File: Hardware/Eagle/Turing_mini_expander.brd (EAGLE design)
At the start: 106 x 19.5 mm, 20 parts, among them U1 TL072_

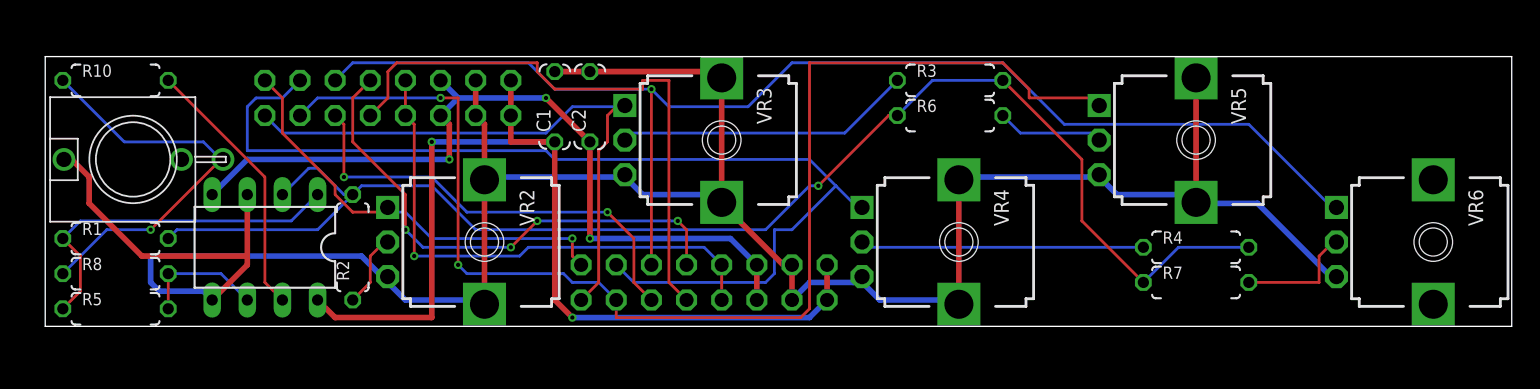
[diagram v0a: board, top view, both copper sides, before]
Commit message: Thonkiconn error corrected and re-routed
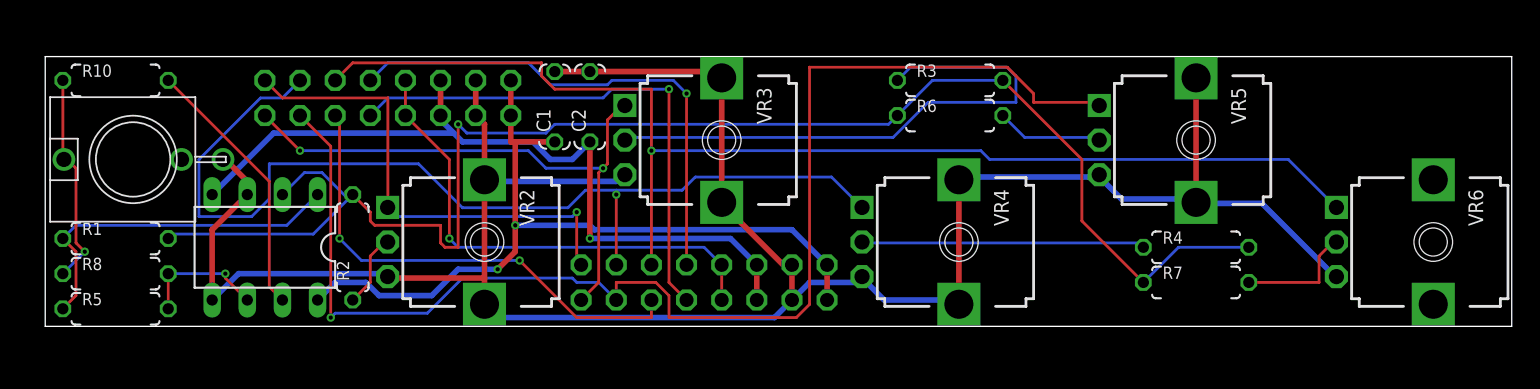
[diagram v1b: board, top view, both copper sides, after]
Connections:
- net GND: now also MAIN_OUT.P$3_SLEEVE; no longer MAIN_OUT.P$1
- net N$5: now also MAIN_OUT.P$1_TIP; no longer MAIN_OUT.P$3
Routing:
- net N$16: track 21.8 -> 40.6 mm
- net +12V: track 72.7 -> 58.3 mm
- net N$5: track 28.9 -> 15.5 mm
- net GND: track 188.0 -> 177.4 mm
- net SUM: track 101.8 -> 108.8 mm
- net GATE8: track 42.5 -> 38.1 mm, vias 0 -> 1
- net GATE1: track 31.4 -> 35.3 mm
- net GATE5: track 92.5 -> 88.6 mm
- net GATE4: track 92.4 -> 95.2 mm, vias 2 -> 1
- net CLOCK: track 38.5 -> 35.8 mm
- net GATE6: track 32.5 -> 35.2 mm
- net GATE3: track 75.0 -> 73.3 mm, vias 0 -> 1
- net GATE2: track 43.0 -> 41.5 mm, vias 0 -> 2
- net -12V: track 58.4 -> 57.0 mm, vias 3 -> 1
- net GATE7: track 37.3 -> 37.0 mm, vias 4 -> 1
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
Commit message: Fixes after first photo
Fixes #2, fixes #3, fixes #4
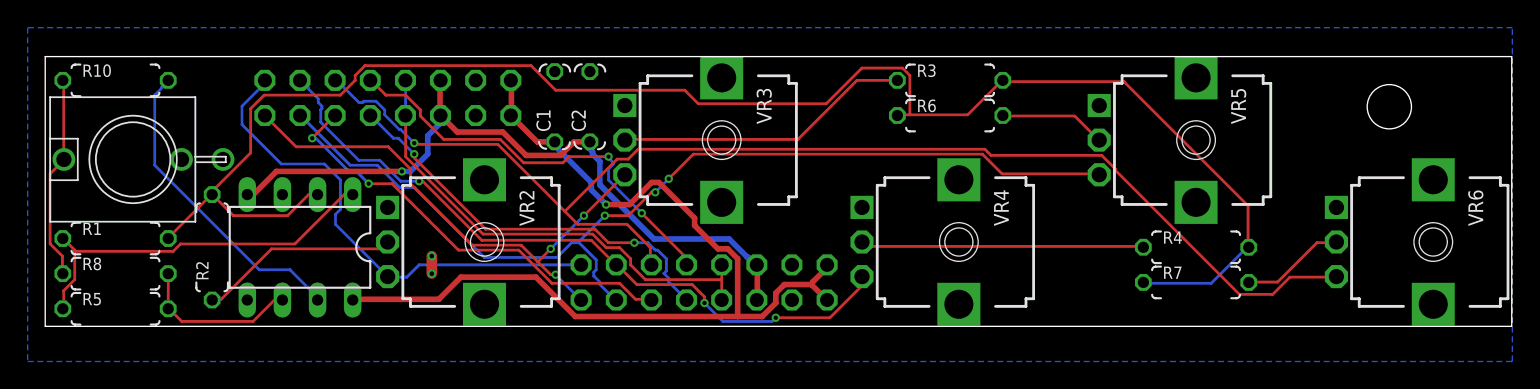
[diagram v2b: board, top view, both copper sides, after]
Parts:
- added U$1: (no value), MusicThingModular:MOUNTING_HOLE
- moved R2 10.2 mm to (12.1, 5.71)
- moved U1 2.54 mm to (18.4, 5.71)
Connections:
- net GATE1: now also VR2.3; no longer VR2.1
- net GATE2: now also VR3.3; no longer VR3.1
- net GATE3: now also VR4.3; no longer VR4.1
- net GATE4: now also VR5.3; no longer VR5.1
- net GATE5: now also VR6.3; no longer VR6.1
- net GND: now also VR2.1, VR2.CHASSIS2, VR3.1, VR3.CHASSIS2, VR4.1, VR4.CHASSIS2, VR5.1, VR5.CHASSIS2, VR6.1, VR6.CHASSIS2; no longer VR2.3, VR2.M1, VR2.M2, VR3.3, VR3.M1, VR3.M2, VR4.3, VR4.M1, VR4.M2, VR5.3, VR5.M1, VR5.M2, VR6.3
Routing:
- net GND: track 177.4 -> 1.27 mm, vias 0 -> 2
- net GATE4: track 95.2 -> 71.2 mm, vias 1 -> 3
- net GATE3: track 73.3 -> 50.8 mm, vias 1 -> 3
- net N$16: track 40.6 -> 21.5 mm
- net +12V: track 58.3 -> 69.5 mm, vias 2 -> 1
- net N$2: track 5.36 -> 14.4 mm
- net GATE8: track 38.1 -> 29.6 mm, vias 1 -> 2
- net SUM: track 108.8 -> 117.2 mm, vias 1 -> 0
- net GATE7: track 37.0 -> 30.6 mm, vias 1 -> 2
- net -12V: track 57.0 -> 52.3 mm
- net GATE2: track 41.5 -> 37.9 mm, vias 2 -> 3
- net GATE6: track 35.2 -> 31.7 mm
- net GATE5: track 88.6 -> 91.9 mm
- net N$6: track 19.3 -> 22.5 mm
- net N$4: track 9.23 -> 11.8 mm, vias 1 -> 0
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- added copper zone on layer 16, net GND
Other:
- board text added: "Turing Machine Mini Voltage Expander Designed in Portscatho Cornwall by Tom Whitwell PCB rev 2 September 2015 musicthing.co.uk"
- board text removed: "Turing Machine Mini Voltage Expander Designed in Portscatho Cornwall by Tom Whitwell PCB rev 1 August 2015 musicthing.co.uk"

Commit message: Add vector logo to back of board
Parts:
- added U$2: (no value), MusicThingModular:MTM_1CM_LOGO_WHITE
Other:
- board text removed: "MUSIC THING MODULAR"

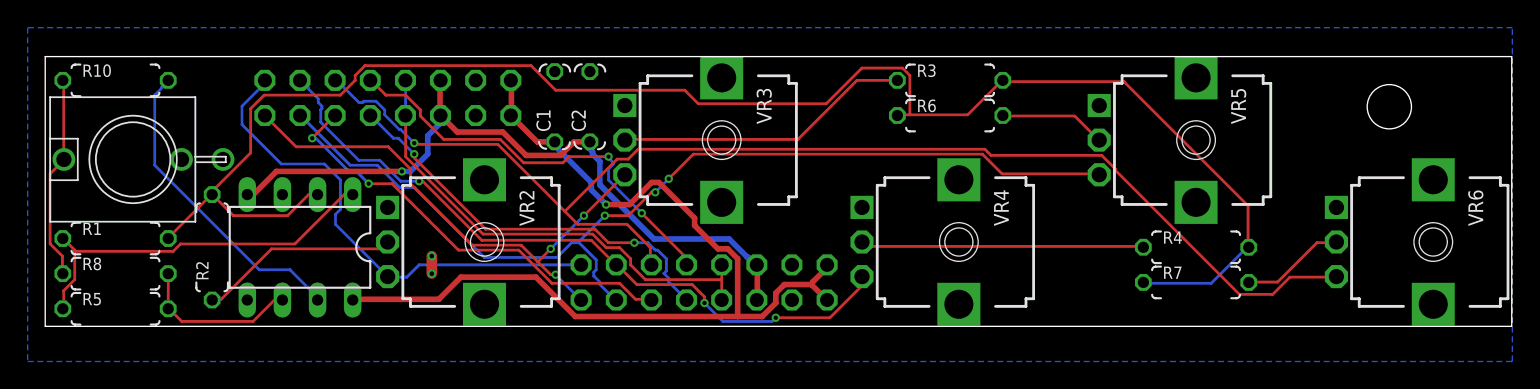
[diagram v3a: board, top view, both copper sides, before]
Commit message: reroute fatter traces
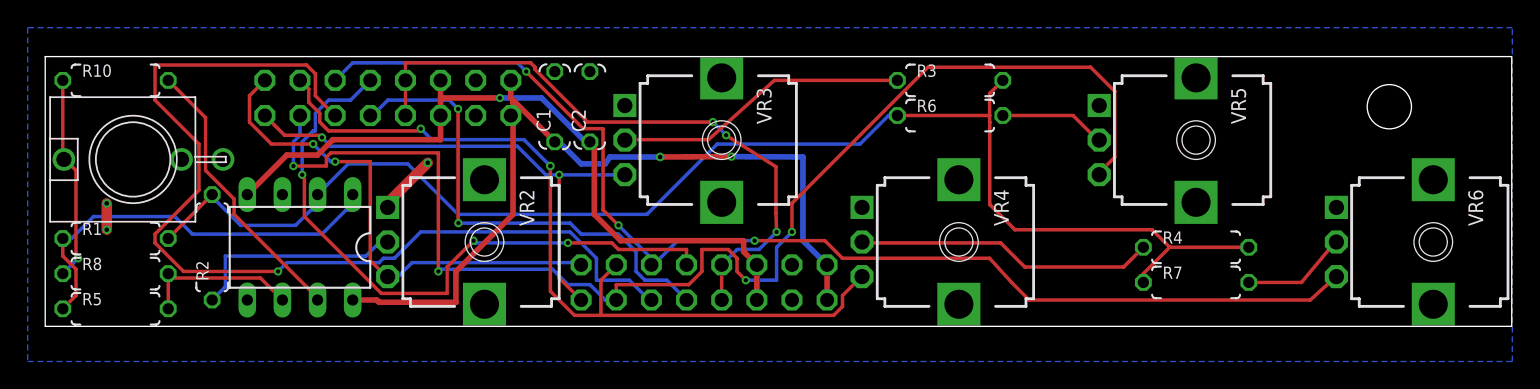
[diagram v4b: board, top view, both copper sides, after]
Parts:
- removed U$2: (no value), MusicThingModular:MTM_1CM_LOGO_WHITE
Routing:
- net GATE6: track 31.7 -> 71.8 mm, vias 2 -> 1
- net GATE4: track 71.2 -> 94.3 mm, vias 3 -> 4
- net GATE7: track 30.6 -> 47.0 mm, vias 2 -> 3
- net SUM: track 117.2 -> 101.4 mm
- net CLOCK: track 34.9 -> 45.8 mm, vias 0 -> 3
- net +12V: track 69.5 -> 59.6 mm, vias 1 -> 2
- net GATE3: track 50.8 -> 59.8 mm, vias 3 -> 2
- net GATE5: track 91.9 -> 85.7 mm, vias 1 -> 3
- net GATE8: track 29.6 -> 35.0 mm
- net GND: track 1.27 -> 6.33 mm, vias 2 -> 3
- net N$15: track 27.6 -> 29.8 mm
- net N$6: track 22.5 -> 20.3 mm
- net -12V: track 52.3 -> 53.6 mm
- net N$2: track 14.4 -> 15.7 mm
- net N$19: track 20.5 -> 21.7 mm
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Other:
- board text added: "RED>> RED>>"
- board text removed: "RED>>RED>>"

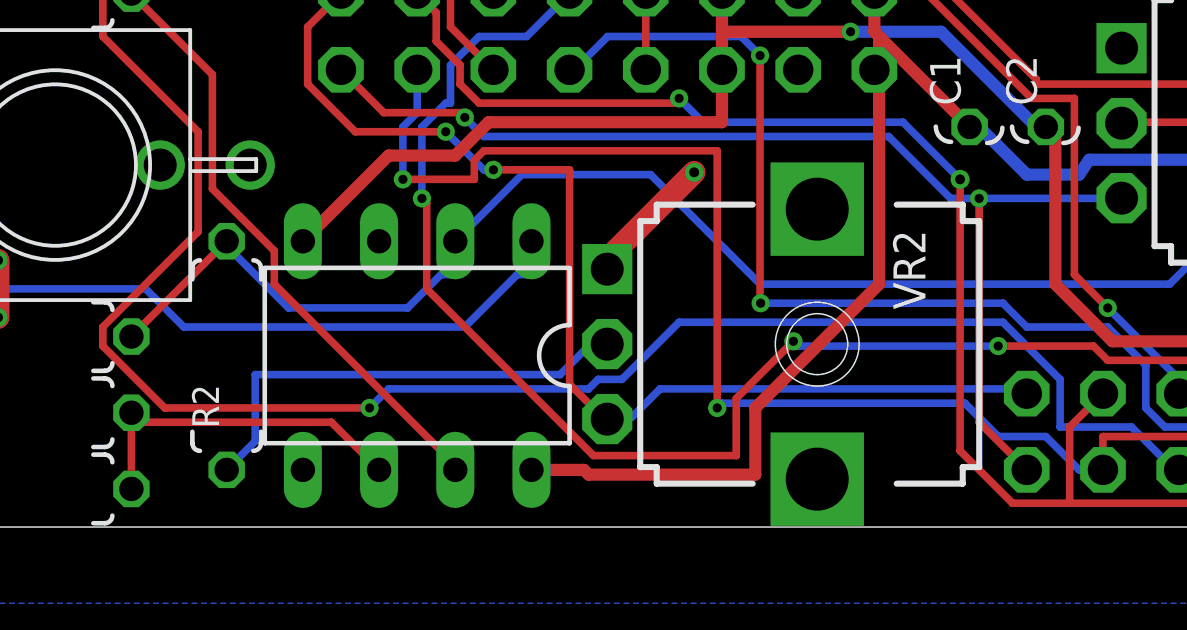
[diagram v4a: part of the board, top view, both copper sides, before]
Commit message: Rev 2 Board and Panel complete and prototypes ordered
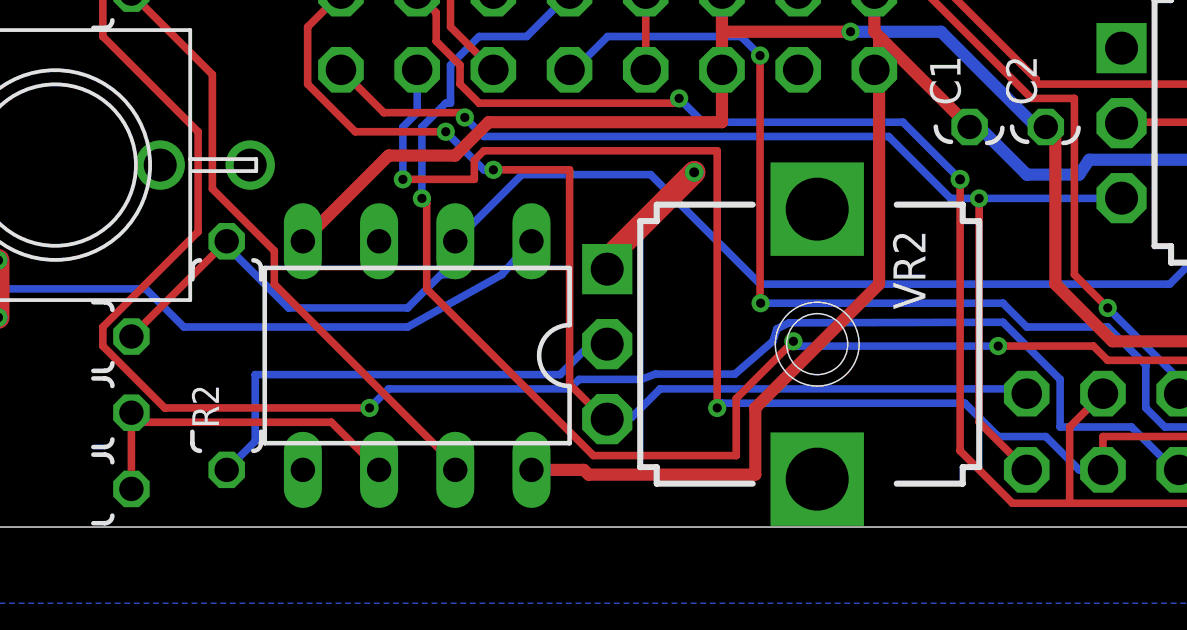
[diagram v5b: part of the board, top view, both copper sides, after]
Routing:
- net N$15: track 29.8 -> 29.0 mm
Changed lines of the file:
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@@
 <setting verticaltext="up"/>
 </settings>
-<grid distance="25" unitdist="mil" unit="mil" style="lines" multiple="1" display="no" altdistance="3.5" altunitdist="mil" altunit="mil"/>
+<grid distance="25" unitdist="mil" unit="mil" style="lines" multiple="1" display="no" altdistance="4" altunitdist="mil" altunit="mil"/>
 <layers>
 <layer number="1" name="Top" color="4" fill="1" visible="yes" active="yes"/>
@@
 <layer number="42" name="bRestrict" color="1" fill="10" visible="yes" active="yes"/>
 <layer number="43" name="vRestrict" color="2" fill="10" visible="yes" active="yes"/>
-<layer number="44" name="Drills" color="7" fill="1" visible="no" active="yes"/>
-<layer number="45" name="Holes" color="7" fill="1" visible="no" active="yes"/>
+<layer number="44" name="Drills" color="7" fill="1" visible="yes" active="yes"/>
+<layer number="45" name="Holes" color="7" fill="1" visible="yes" active="yes"/>
 <layer number="46" name="Milling" color="3" fill="1" visible="yes" active="yes"/>
 <layer number="47" name="Measures" color="7" fill="1" visible="yes" active="yes"/>
@@
 <wire x1="106" y1="19.5" x2="0" y2="19.5" width="0" layer="20"/>
 <wire x1="0" y1="19.5" x2="0" y2="0" width="0" layer="20"/>
-<text x="11.267440625" y="18.93061875" size="1.27" layer="22" font="vector" ratio="15" rot="SMR270" align="top-left">RED&gt;&gt;
+<text x="13.807440625" y="13.85061875" size="1.27" layer="22" font="vector" ratio="15" rot="SMR90" align="top-left">RED&gt;&gt;
 RED&gt;&gt;</text>
 <text x="92.32265" y="0.27305" size="1.016" layer="22" font="vector" rot="SMR90" align="top-left">Turing Machine
@@
 DO NOT CONNECT
 TO CASE POWER</text>
-<text x="34.127440625" y="5.59561875" size="1.27" layer="22" font="vector" ratio="15" rot="SMR270" align="top-left">RED&gt;&gt;
+<text x="36.667440625" y="0.51561875" size="1.27" layer="22" font="vector" ratio="15" rot="SMR90" align="top-left">RED&gt;&gt;
 RED&gt;&gt;</text>
 <text x="52.705" y="7.62" size="1.016" layer="22" rot="SMR90">Either header
 will work! </text>
-<polygon width="0" layer="22">
+<polygon width="0.0508" layer="22">
 <vertex x="71.42605625" y="18.5256625"/>
 <vertex x="70.942440625" y="18.5256625"/>
@@
 <vertex x="71.434690625" y="18.517028125"/>
 </polygon>
-<polygon width="0" layer="22">
+<polygon width="0.0508" layer="22">
 <vertex x="71.521053125" y="15.865775"/>
 <vertex x="71.50378125" y="15.632603125"/>
@@
 <vertex x="71.49514375" y="15.883046875"/>
 </polygon>
-<polygon width="0" layer="22">
+<polygon width="0.0508" layer="22">
 <vertex x="67.81620625" y="15.883046875"/>
 <vertex x="68.377546875" y="15.883046875"/>
@@
 <vertex x="67.81620625" y="15.891684375"/>
 </polygon>
-<polygon width="0" layer="22">
+<polygon width="0.0508" layer="22">
 <vertex x="72.617825" y="14.199028125"/>
 <vertex x="67.81620625" y="14.199028125"/>
@@
 <vertex x="72.617825" y="13.335428125"/>
 </polygon>
-<polygon width="0" layer="22">
+<polygon width="0.0508" layer="22">
 <vertex x="68.230734375" y="12.143659375"/>
 <vertex x="67.9975625" y="11.988209375"/>
@@
 <vertex x="68.2134625" y="12.135021875"/>
 </polygon>
-<polygon width="0" layer="22">
+<polygon width="0.0508" layer="22">
 <vertex x="72.617825" y="9.362865625"/>
 <vertex x="71.0978875" y="9.362865625"/>
@@
 <vertex x="72.6091875" y="9.371503125"/>
 </polygon>
-<polygon width="0" layer="22">
+<polygon width="0.0508" layer="22">
 <vertex x="67.764390625" y="8.87925"/>
 <vertex x="68.4293625" y="8.87925"/>
@@
 <vertex x="67.7816625" y="8.87925"/>
 </polygon>
-<polygon width="0" layer="22">
+<polygon width="0.0508" layer="22">
 <vertex x="71.512415625" y="6.04664375"/>
 <vertex x="70.873353125" y="6.04664375"/>
@@
 <vertex x="71.50378125" y="6.055278125"/>
 </polygon>
-<polygon width="0" layer="22">
+<polygon width="0.0508" layer="22">
 <vertex x="71.512415625" y="6.04664375"/>
 <vertex x="71.48650625" y="5.7875625"/>
@@
 <vertex x="70.85608125" y="6.04664375"/>
 </polygon>
-<polygon width="0" layer="22">
+<polygon width="0.0508" layer="22">
 <vertex x="72.617825" y="1.78909375"/>
 <vertex x="71.48650625" y="2.00499375"/>
@@
 <vertex x="72.617825" y="0.441878125"/>
 </polygon>
-<polygon width="0" layer="22">
+<polygon width="0.0508" layer="22">
 <vertex x="73.049625" y="11.815490625"/>
 <vertex x="73.749140625" y="11.815490625"/>
@@
 <vertex x="73.049625" y="11.8414"/>
 </polygon>
-<polygon width="0" layer="22">
+<polygon width="0.0508" layer="22">
 <vertex x="73.049625" y="11.815490625"/>
 <vertex x="73.058259375" y="11.8414"/>
@@
 <vertex x="73.08416875" y="11.780946875"/>
 </polygon>
-<polygon width="0" layer="22">
+<polygon width="0.0508" layer="22">
 <vertex x="76.60765625" y="8.499265625"/>
 <vertex x="76.184490625" y="8.499265625"/>
@@
 <vertex x="76.6335625" y="8.5165375"/>
 </polygon>
-<polygon width="0" layer="22">
+<polygon width="0.0508" layer="22">
 <vertex x="76.60765625" y="7.18659375"/>
 <vertex x="72.980534375" y="7.18659375"/>
@@
 <vertex x="76.60765625" y="6.32299375"/>
 </polygon>
-<polygon width="0" layer="22">
+<polygon width="0.0508" layer="22">
 <vertex x="77.851240625" y="7.18659375"/>
 <vertex x="77.056728125" y="7.18659375"/>
@@
 <vertex x="77.851240625" y="6.32299375"/>
 </polygon>
-<polygon width="0" layer="22">
+<polygon width="0.0508" layer="22">
 <vertex x="77.7907875" y="4.146721875"/>
 <vertex x="76.23630625" y="4.146721875"/>
@@
 <vertex x="77.799425" y="4.16399375"/>
 </polygon>
-<polygon width="0" layer="22">
+<polygon width="0.0508" layer="22">
 <vertex x="76.996275" y="3.04995"/>
 <vertex x="76.996275" y="2.074084375"/>
@@
 <vertex x="77.7907875" y="3.04995"/>
 </polygon>
-<polygon width="0" layer="22">
+<polygon width="0.0508" layer="22">
 <vertex x="80.7443" y="13.680865625"/>
 <vertex x="80.977471875" y="13.620415625"/>
@@
 <vertex x="80.7356625" y="13.689503125"/>
 </polygon>
-<polygon width="0" layer="22">
+<polygon width="0.0508" layer="22">
 <vertex x="81.78925625" y="11.47005"/>
 <vertex x="78.162134375" y="11.47005"/>
@@
 <vertex x="81.78925625" y="10.60645"/>
 </polygon>
-<polygon width="0" layer="22">
+<polygon width="0.0508" layer="22">
 <vertex x="83.032840625" y="11.47005"/>
 <vertex x="82.238328125" y="11.47005"/>
@@
 <vertex x="83.032840625" y="10.60645"/>
 </polygon>
-<polygon width="0" layer="22">
+<polygon width="0.0508" layer="22">
 <vertex x="79.233" y="8.430178125"/>
 <vertex x="79.0171" y="8.4560875"/>
@@
 <vertex x="79.215728125" y="8.404271875"/>
 </polygon>
-<polygon width="0" layer="22">
+<polygon width="0.0508" layer="22">
 <vertex x="78.593934375" y="6.633890625"/>
 <vertex x="78.3607625" y="6.47844375"/>
@@
 <vertex x="78.5766625" y="6.62525625"/>
 </polygon>
-<polygon width="0" layer="22">
+<polygon width="0.0508" layer="22">
 <vertex x="82.9723875" y="1.78909375"/>
 <vertex x="79.578440625" y="2.43679375"/>
@@
 <wire x1="16.8275" y1="3.96875" x2="10.00125" y2="3.96875" width="0.254" layer="1"/>
 <wire x1="17.4625" y1="4.60375" x2="16.8275" y2="3.96875" width="0.254" layer="16"/>
-<wire x1="24.13" y1="4.60375" x2="17.4625" y2="4.60375" width="0.254" layer="16"/>
-<wire x1="24.4475" y1="4.92125" x2="24.13" y2="4.60375" width="0.254" layer="16"/>
-<wire x1="25.24125" y1="4.92125" x2="24.4475" y2="4.92125" width="0.254" layer="16"/>
-<wire x1="27.14625" y1="6.82625" x2="25.24125" y2="4.92125" width="0.254" layer="16"/>
-<wire x1="37.94125" y1="6.82625" x2="27.14625" y2="6.82625" width="0.254" layer="16"/>
+<wire x1="23.495" y1="4.60375" x2="17.4625" y2="4.60375" width="0.254" layer="16"/>
+<wire x1="23.8125" y1="4.92125" x2="23.495" y2="4.60375" width="0.254" layer="16"/>
+<wire x1="25.87625" y1="4.92125" x2="23.8125" y2="4.92125" width="0.254" layer="16"/>
+<wire x1="26.35885" y1="5.09905" x2="25.87625" y2="4.92125" width="0.254" layer="16"/>
+<wire x1="37.94125" y1="6.82625" x2="30.8102" y2="6.8072" width="0.254" layer="16"/>
+<wire x1="30.8102" y1="6.8072" x2="30.4038" y2="6.604" width="0.254" layer="16"/>
+<wire x1="30.4038" y1="6.604" x2="30.2768" y2="6.1976" width="0.254" layer="16"/>
+<wire x1="30.2768" y1="6.1976" x2="29.0068" y2="5.09905" width="0.254" layer="16"/>
+<wire x1="29.0068" y1="5.09905" x2="26.35885" y2="5.09905" width="0.254" layer="16"/>
 <wire x1="39.84625" y1="4.92125" x2="37.94125" y2="6.82625" width="0.254" layer="16"/>
 <wire x1="39.84625" y1="3.33375" x2="39.84625" y2="4.92125" width="0.254" layer="16"/>
@@
 <wire x1="1.27" y1="5.08" x2="2.2225" y2="4.1275" width="0.254" layer="1"/>
 <wire x1="1.27" y1="6.35" x2="1.27" y2="5.08" width="0.254" layer="1"/>
-<wire x1="22.225" y1="8.41375" x2="22.225" y2="9.525" width="0.254" layer="16"/>
-<wire x1="21.74875" y1="8.41375" x2="22.225" y2="8.41375" width="0.254" layer="16"/>
-<wire x1="20.0025" y1="6.6675" x2="21.74875" y2="8.41375" width="0.254" layer="16"/>
-<wire x1="10.63625" y1="6.6675" x2="20.0025" y2="6.6675" width="0.254" layer="16"/>
+<wire x1="22.225" y1="9.53135" x2="22.225" y2="9.525" width="0.254" layer="16"/>
+<wire x1="21.24075" y1="8.41375" x2="22.225" y2="9.53135" width="0.254" layer="16"/>
+<wire x1="18.0975" y1="6.6675" x2="21.24075" y2="8.41375" width="0.254" layer="16"/>
+<wire x1="10.63625" y1="6.6675" x2="18.0975" y2="6.6675" width="0.254" layer="16"/>
 <wire x1="9.36625" y1="7.9375" x2="10.63625" y2="6.6675" width="0.254" layer="16"/>
 <wire x1="3.4925" y1="7.9375" x2="9.36625" y2="7.9375" width="0.254" layer="16"/>
